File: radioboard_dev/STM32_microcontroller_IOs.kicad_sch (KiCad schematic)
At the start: 20 parts, among them U10 STM32WL55CCUx

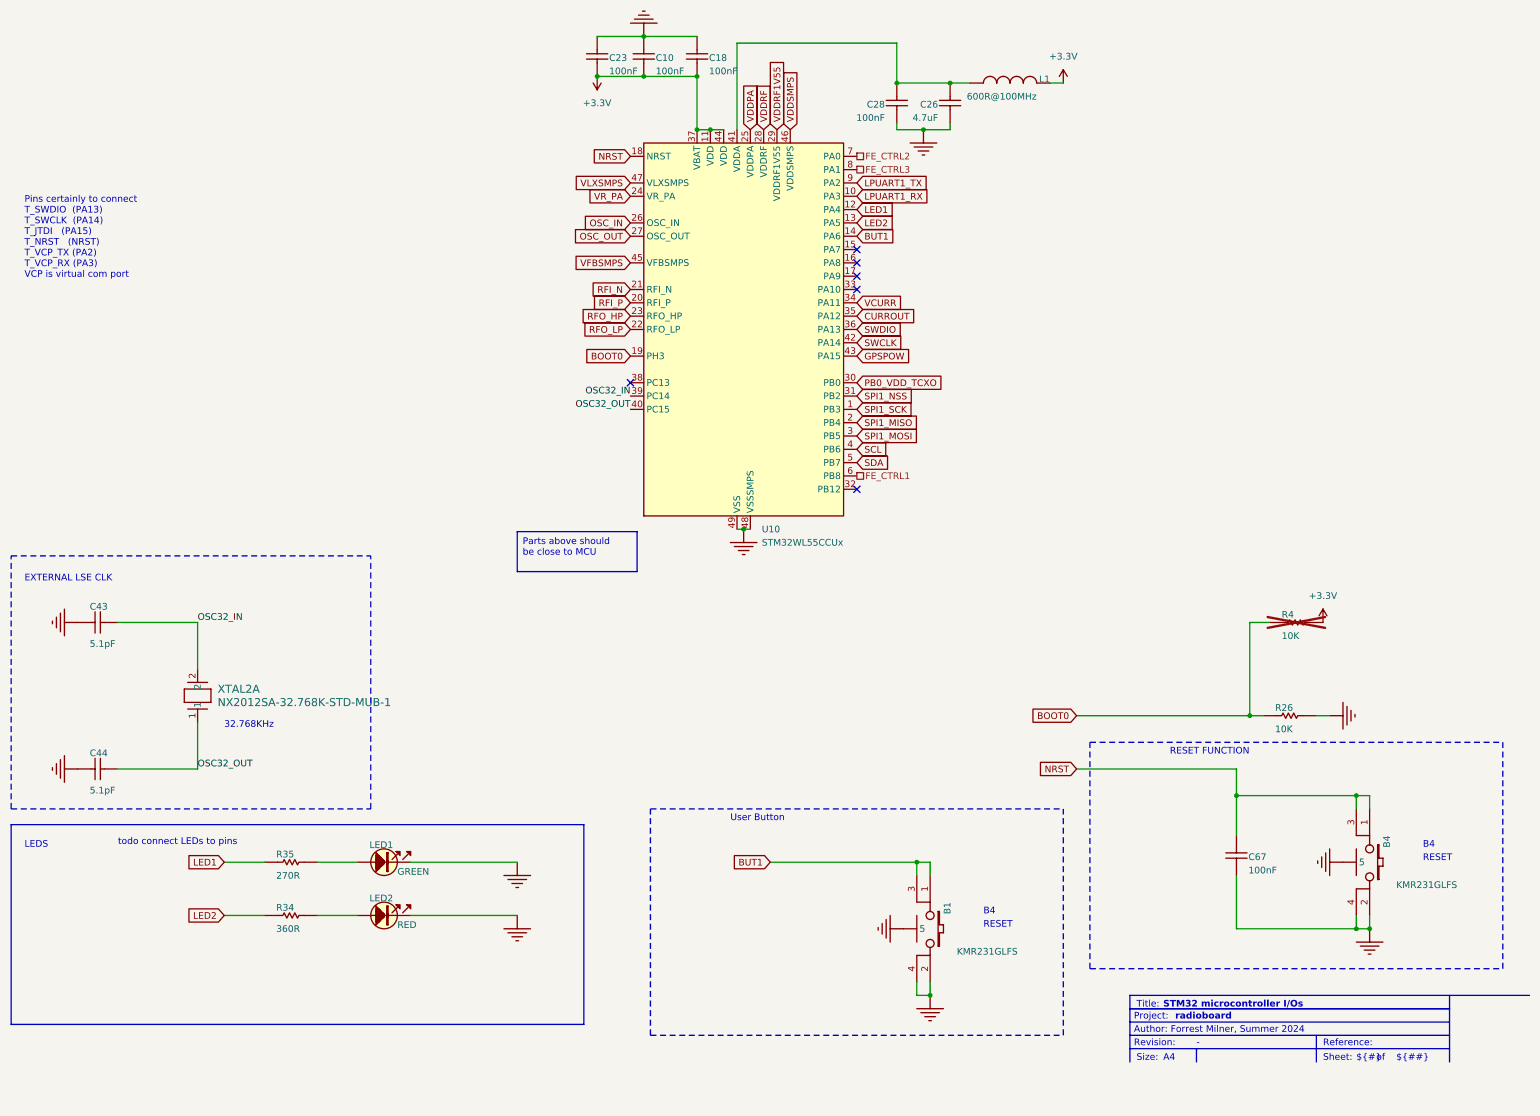
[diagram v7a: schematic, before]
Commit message: bom changes
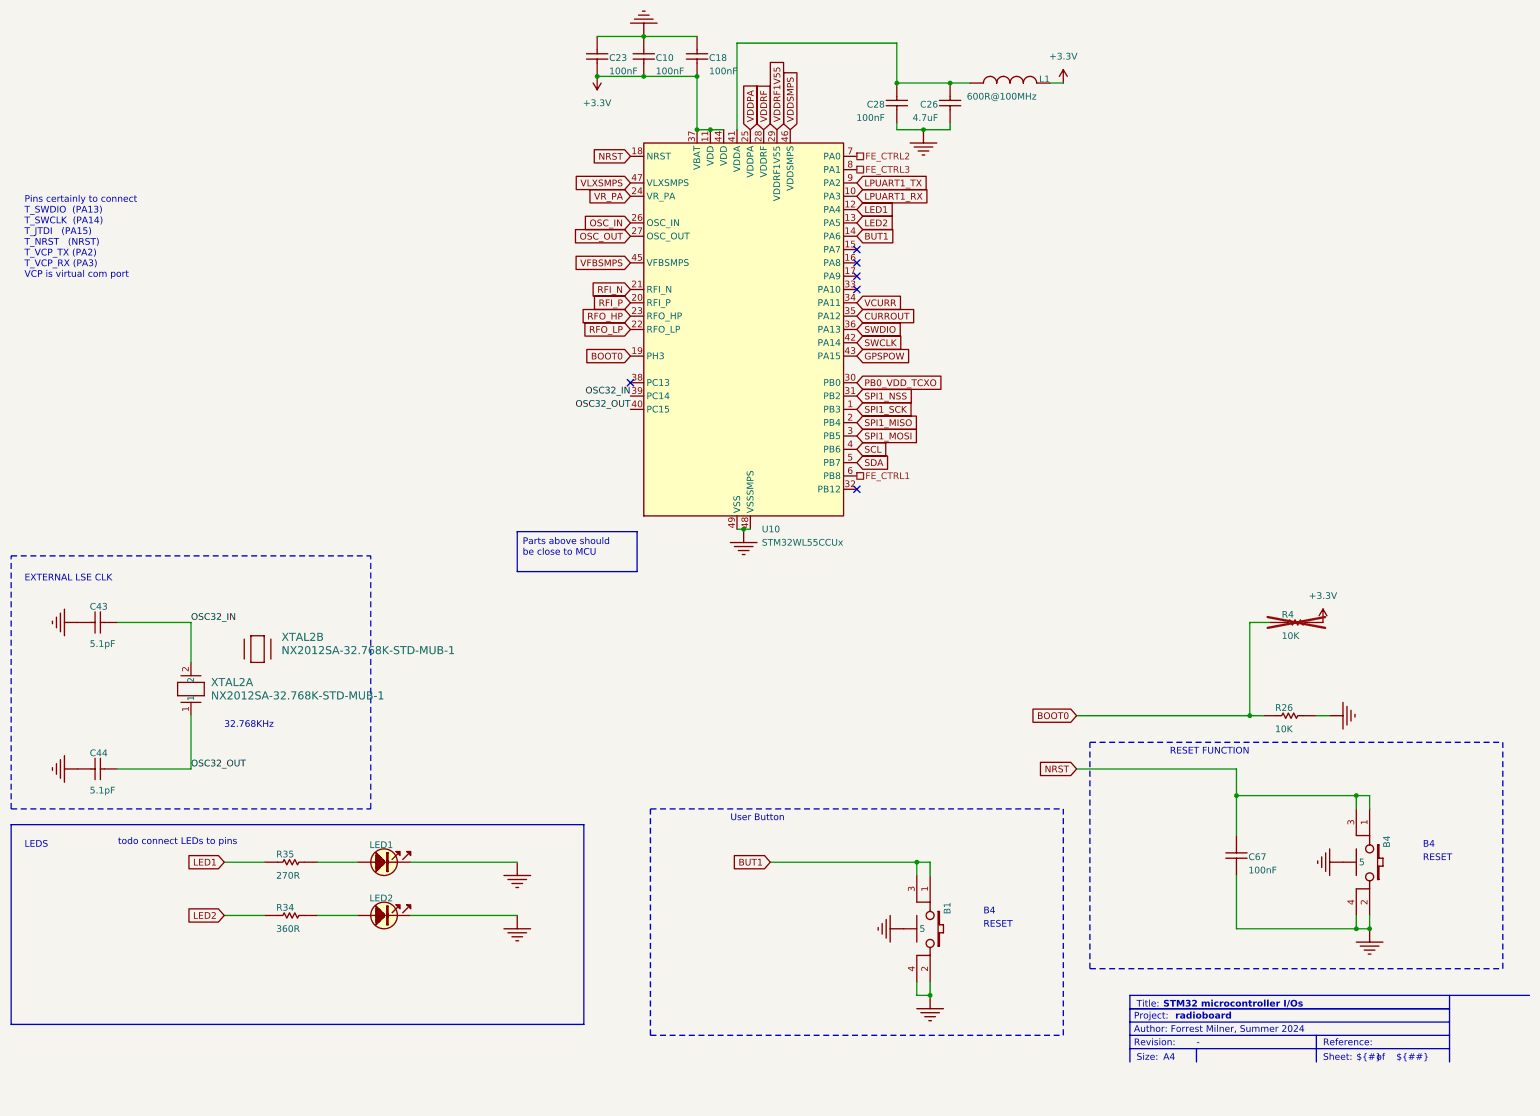
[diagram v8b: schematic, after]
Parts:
- added unit 2 of XTAL2
- B1, B4: ALTIUM_VALUE KMR231GLFS -> (none); COMPONENTLINK1DESCRIPTION Datasheet -> (none); COMPONENTLINK1URL http://tunmcdsvn.tun.st.com/Component_Datasheet_Library/Tru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 -> (none); ECCN_EU n/a -> (none); ECCN_US n/a -> (none); INTERNAL_PART_NUMBER MCD-01485 -> (none); MANUFACTURER C&K -> (none); MANUFACTURER_PART_NUMBER KMR231GLFS -> (none); PART_TYPE Misc -> (none); PROVIDED_BY SUBCO -> (none); STATUS Checked -> (none)
- LED1: ALTERNATE_MANUFACTURER VISHAY SEMICONDUCTOR OPTO DIVISION -> (none); ALTERNATE_MANUFACTURER_PART_NUMBER VLMTG1300-GS08 -> (none); ALTIUM_VALUE GREEN -> (none); COMPONENTLINK1DESCRIPTION Datasheet -> (none); COMPONENTLINK1URL http://tunmcdsvn.tun.st.com/Component_Datasheet_Library/Tru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 -> (none); ECCN_EU n/a -> (none); ECCN_US n/a -> (none); INTERNAL_PART_NUMBER MCD-00588 -> (none); MANUFACTURER OSRAM OPTO SEMICONDUCTORS -> (none); MANUFACTURER_PART_NUMBER LG Q396-PS-35 -> (none); ORDER_CODE_DIGIKEY LG Q396-PS-35-ND -> (none); PACKAGE LED 0603 -> (none); PART_TYPE Display -> (none); PROVIDED_BY SUBCO -> (none); STATUS Released -> (none)
- LED2: ALTERNATE_MANUFACTURER OSRAM OPTO SEMICONDUCTORS -> (none); ALTERNATE_MANUFACTURER_PART_NUMBER LS Q976-NR-1 -> (none); ALTIUM_VALUE RED -> (none); COMPONENTLINK1DESCRIPTION Datasheet -> (none); COMPONENTLINK1URL http://tunmcdsvn.tun.st.com/Component_Datasheet_Library/Tru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 -> (none); ECCN_EU n/a -> (none); ECCN_US n/a -> (none); INTERNAL_PART_NUMBER MCD-00587 -> (none); MANUFACTURER VISHAY -> (none); MANUFACTURER_PART_NUMBER VLMS1300-GS08 -> (none); ORDER_CODE_DIGIKEY VLMS1300-GS08CT-ND -> (none); ORDER_CODE_FARNELL 2078728 -> (none); PACKAGE LED 0603 -> (none); PART_TYPE Display -> (none); PROVIDED_BY SUBCO -> (none); STATUS Released -> (none)
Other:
- moved on the sheet: XTAL2A
